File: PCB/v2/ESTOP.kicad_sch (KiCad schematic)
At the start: 10 parts

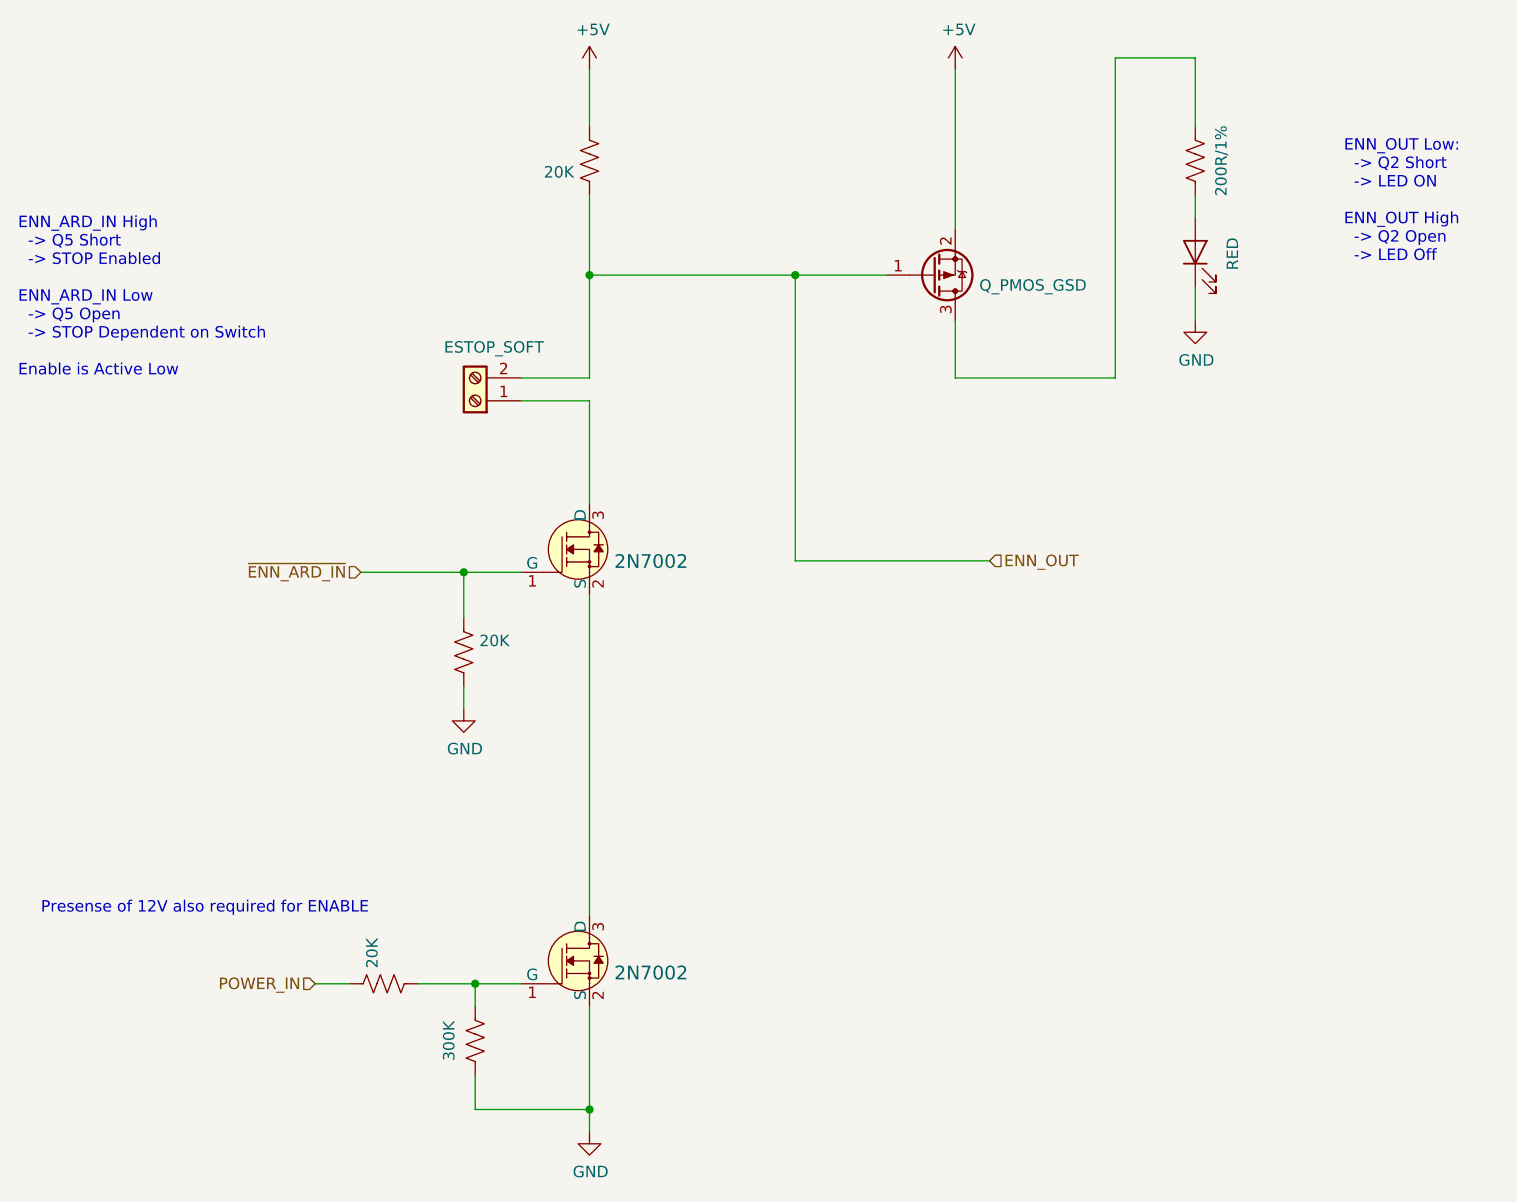
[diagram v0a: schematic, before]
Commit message: WIP updated symbols for tmc5106
Updated footprint for tmc5106,
need to check how motor wiring is done, might be wired up stupid before and that's gonna be sad
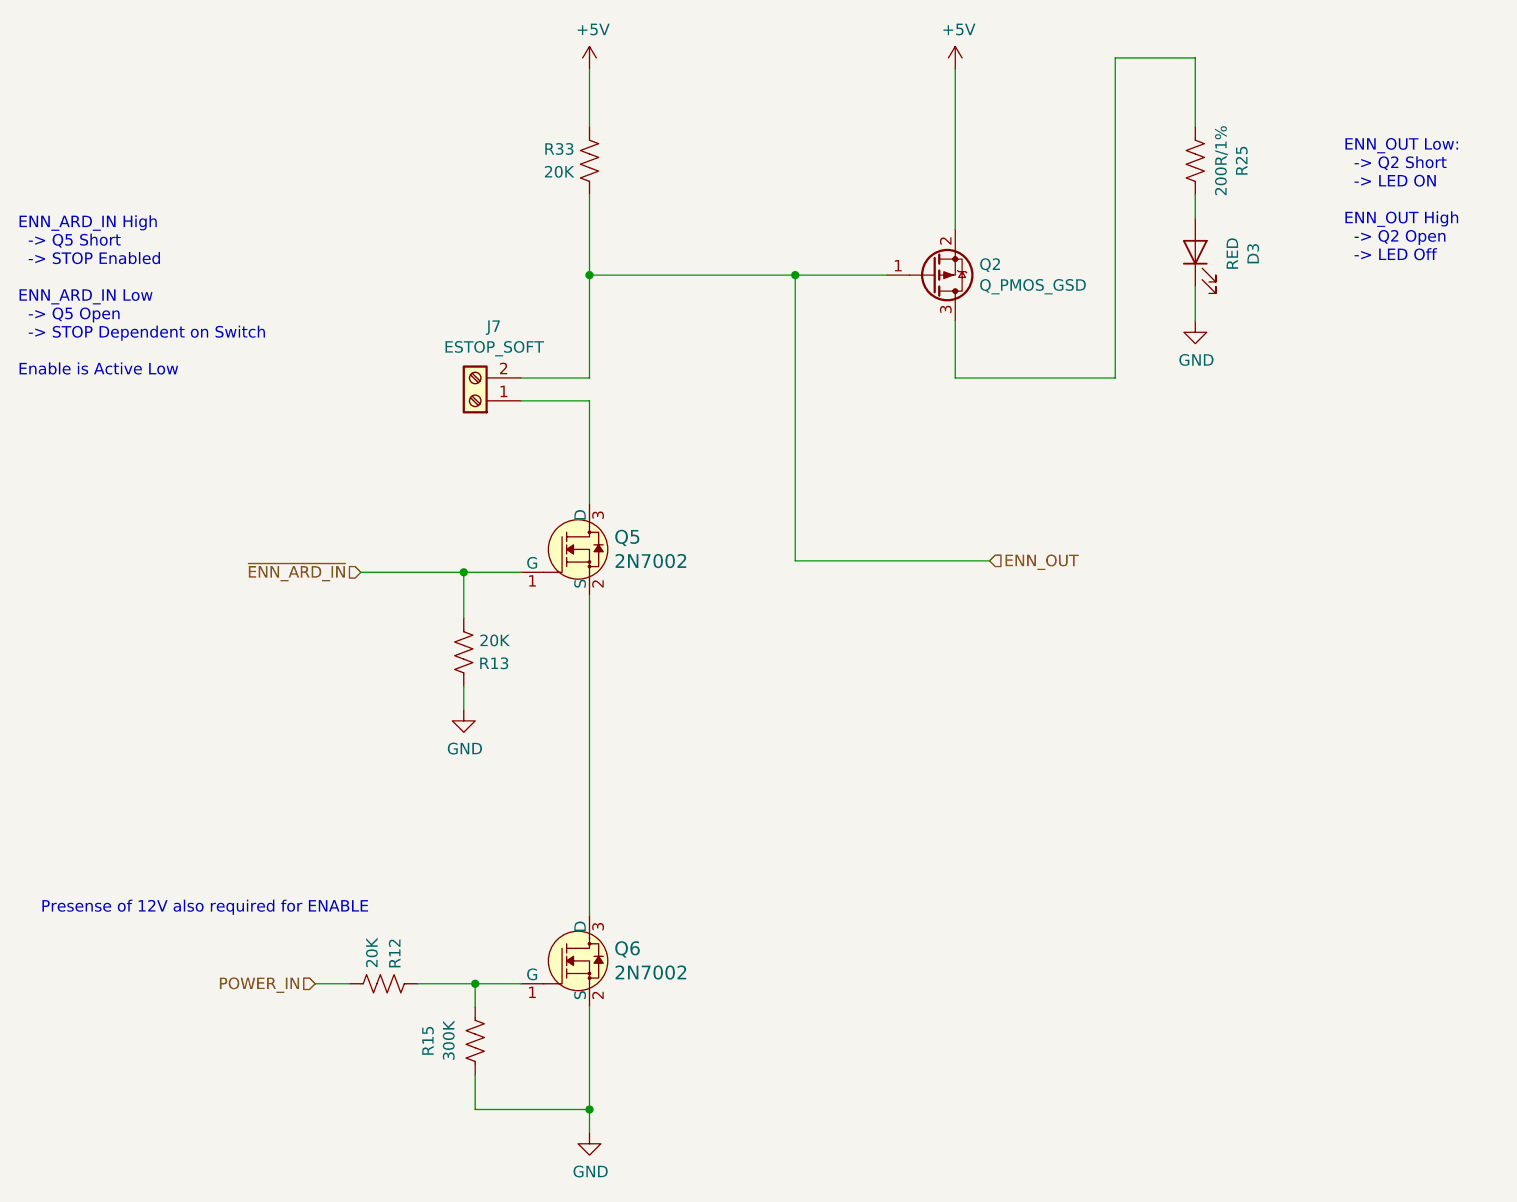
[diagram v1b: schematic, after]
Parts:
- gave numbers to parts that had none: 10
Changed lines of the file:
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@@
   (symbol (lib_id "MMTK-rescue:+5V-power-MMTK-rescue-MMTK-rescue") (at 153.67 34.29 0) (unit 1)
     (in_bom yes) (on_board yes)
-    (property "Reference" "" (id 0) (at 153.67 38.1 0)
+    (property "Reference" "#PWR0150" (id 0) (at 153.67 38.1 0)
       (effects (font (size 1.27 1.27)) hide)
     )
@@
   (symbol (lib_id "MMTK-rescue:Q_PMOS_GSD-Device-MMTK-rescue-MMTK-rescue") (at 151.13 57.15 0) (mirror x) (unit 1)
     (in_bom yes) (on_board yes)
-    (property "Reference" "" (id 0) (at 156.337 55.9816 0)
+    (property "Reference" "Q2" (id 0) (at 156.337 55.9816 0)
       (effects (font (size 1.27 1.27)) (justify left))
     )
@@
   (symbol (lib_id "MMTK-rescue:Screw_Terminal_01x02-Connector-MMTK-rescue-MMTK-rescue") (at 100.33 71.12 180) (unit 1)
     (in_bom yes) (on_board yes)
-    (property "Reference" "" (id 0) (at 102.4128 62.865 0))
+    (property "Reference" "J7" (id 0) (at 102.4128 62.865 0))
     (property "Value" "ESTOP_SOFT" (id 1) (at 102.4128 65.1764 0))
     (property "Footprint" "TerminalBlock_Phoenix:TerminalBlock_Phoenix_PT-1,5-2-3.5-H_1x02_P3.50mm_Horizontal" (id 2) (at 100.33 71.12 0)
@@
   (symbol (lib_id "MMTK-rescue:+5V-power-MMTK-rescue-MMTK-rescue") (at 113.03 34.29 0) (unit 1)
     (in_bom yes) (on_board yes)
-    (property "Reference" "" (id 0) (at 113.03 38.1 0)
+    (property "Reference" "#PWR0151" (id 0) (at 113.03 38.1 0)
       (effects (font (size 1.27 1.27)) hide)
     )
@@
   (symbol (lib_id "MMTK-rescue:LED-Device-MMTK-rescue-MMTK-rescue") (at 180.34 54.61 90) (unit 1)
     (in_bom yes) (on_board yes)
-    (property "Reference" "" (id 0) (at 186.817 54.7878 0))
+    (property "Reference" "D3" (id 0) (at 186.817 54.7878 0))
     (property "Value" "RED" (id 1) (at 184.5056 54.7878 0))
     (property "Footprint" "LED_SMD:LED_0603_1608Metric" (id 2) (at 180.34 54.61 0)
@@
   (symbol (lib_id "MMTK-rescue:R_US-Device-MMTK-rescue-MMTK-rescue") (at 180.34 44.45 180) (unit 1)
     (in_bom yes) (on_board yes)
-    (property "Reference" "" (id 0) (at 185.547 44.45 90))
+    (property "Reference" "R25" (id 0) (at 185.547 44.45 90))
     (property "Value" "200R/1%" (id 1) (at 183.2356 44.45 90))
     (property "Footprint" "Resistor_SMD:R_0603_1608Metric" (id 2) (at 179.324 44.196 90)
@@
   (symbol (lib_id "MMTK-rescue:GND-power-MMTK-rescue-MMTK-rescue") (at 180.34 62.23 0) (unit 1)
     (in_bom yes) (on_board yes)
-    (property "Reference" "" (id 0) (at 180.34 68.58 0)
+    (property "Reference" "#PWR0157" (id 0) (at 180.34 68.58 0)
       (effects (font (size 1.27 1.27)) hide)
     )
@@
   (symbol (lib_id "MMTK-rescue:R_US-Device-MMTK-rescue-MMTK-rescue") (at 113.03 44.45 180) (unit 1)
     (in_bom yes) (on_board yes)
-    (property "Reference" "" (id 0) (at 107.95 43.18 0)
+    (property "Reference" "R33" (id 0) (at 107.95 43.18 0)
       (effects (font (size 1.27 1.27)) (justify right))
     )
@@
   (symbol (lib_id "dk_Transistors-FETs-MOSFETs-Single:2N7002") (at 113.03 87.63 0) (unit 1)
     (in_bom yes) (on_board yes)
-    (property "Reference" "" (id 0) (at 115.7732 86.2838 0)
+    (property "Reference" "Q5" (id 0) (at 115.7732 86.2838 0)
       (effects (font (size 1.524 1.524)) (justify left))
     )
@@
   (symbol (lib_id "MMTK-rescue:GND-power-MMTK-rescue-MMTK-rescue") (at 113.03 152.4 0) (unit 1)
     (in_bom yes) (on_board yes)
-    (property "Reference" "" (id 0) (at 113.03 158.75 0)
+    (property "Reference" "#PWR0158" (id 0) (at 113.03 158.75 0)
       (effects (font (size 1.27 1.27)) hide)
     )
@@
   (symbol (lib_id "dk_Transistors-FETs-MOSFETs-Single:2N7002") (at 113.03 133.35 0) (unit 1)
     (in_bom yes) (on_board yes)
-    (property "Reference" "" (id 0) (at 115.7732 132.0038 0)
+    (property "Reference" "Q6" (id 0) (at 115.7732 132.0038 0)
       (effects (font (size 1.524 1.524)) (justify left))
     )
@@
   (symbol (lib_id "MMTK-rescue:R_US-Device-MMTK-rescue-MMTK-rescue") (at 90.17 135.89 90) (unit 1)
     (in_bom yes) (on_board yes)
-    (property "Reference" "" (id 0) (at 91.44 130.81 0)
+    (property "Reference" "R12" (id 0) (at 91.44 130.81 0)
       (effects (font (size 1.27 1.27)) (justify right))
     )
@@
   (symbol (lib_id "MMTK-rescue:R_US-Device-MMTK-rescue-MMTK-rescue") (at 100.33 142.24 0) (unit 1)
     (in_bom yes) (on_board yes)
-    (property "Reference" "" (id 0) (at 95.123 142.24 90))
+    (property "Reference" "R15" (id 0) (at 95.123 142.24 90))
     (property "Value" "300K" (id 1) (at 97.4344 142.24 90))
     (property "Footprint" "Resistor_SMD:R_0603_1608Metric" (id 2) (at 101.346 142.494 90)
@@
   (symbol (lib_id "MMTK-rescue:R_US-Device-MMTK-rescue-MMTK-rescue") (at 99.06 99.06 0) (unit 1)
     (in_bom yes) (on_board yes)
-    (property "Reference" "" (id 0) (at 104.14 100.33 0)
+    (property "Reference" "R13" (id 0) (at 104.14 100.33 0)
       (effects (font (size 1.27 1.27)) (justify right))
     )
@@
   (symbol (lib_id "MMTK-rescue:GND-power-MMTK-rescue-MMTK-rescue") (at 99.06 105.41 0) (unit 1)
     (in_bom yes) (on_board yes)
-    (property "Reference" "" (id 0) (at 99.06 111.76 0)
-      (effects (font (size 1.27 1.27)) hide)
-    )
+    (property "Reference" "#PWR0122" (id 0) (at 99.06 111.76 0)
+      (effects (font (size 1.27 1.27)) hide)
+    )
